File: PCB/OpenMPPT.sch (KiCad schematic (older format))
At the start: 42 parts, among them J101 THERM, J103 XT60, J104 XT60, Q101 FDMS8050, Q102 FDMS8050, Q103 FDMS8050, Q104 FDMS8050, U101 BQ24650

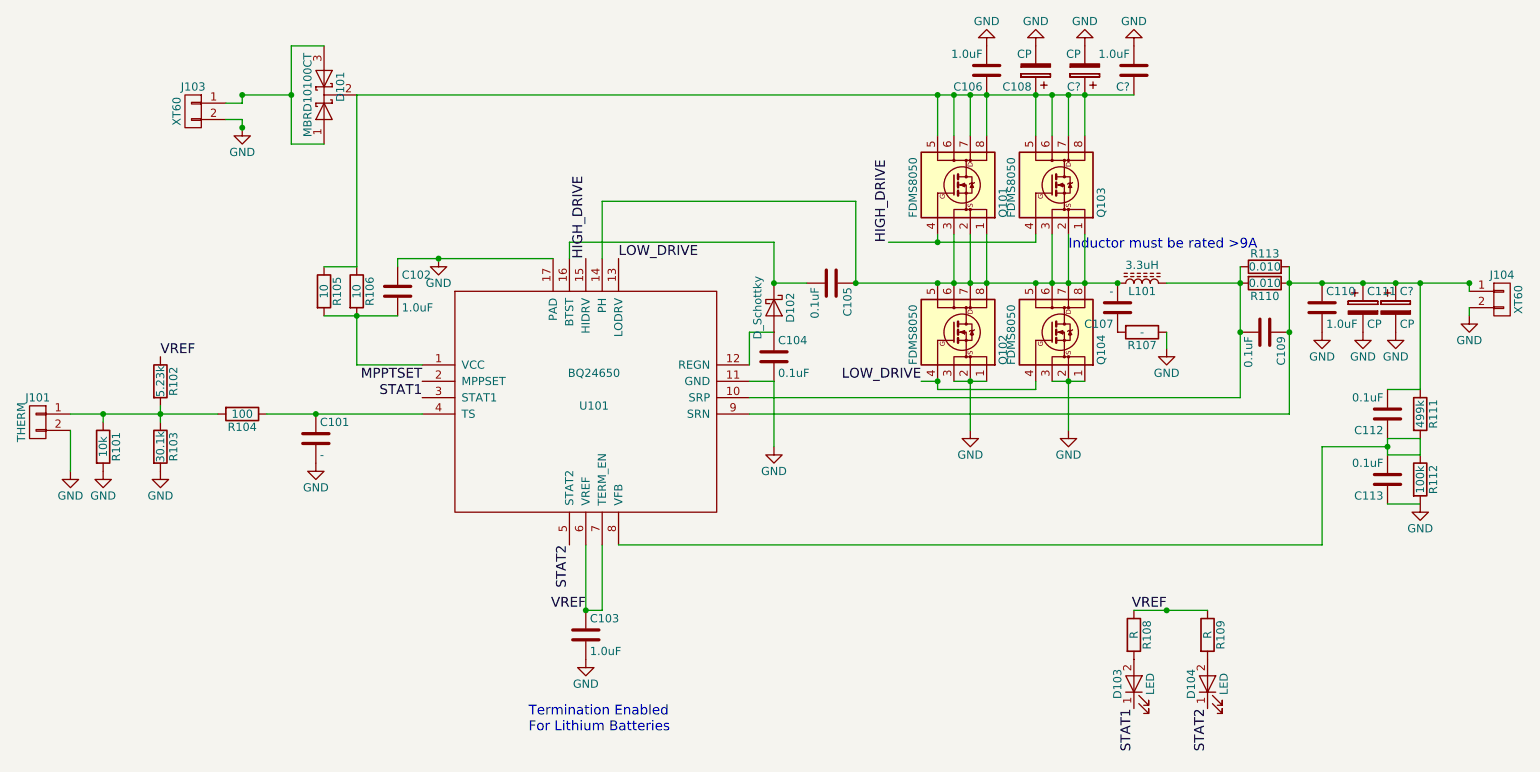
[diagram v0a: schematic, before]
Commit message: Add MPPT resistors
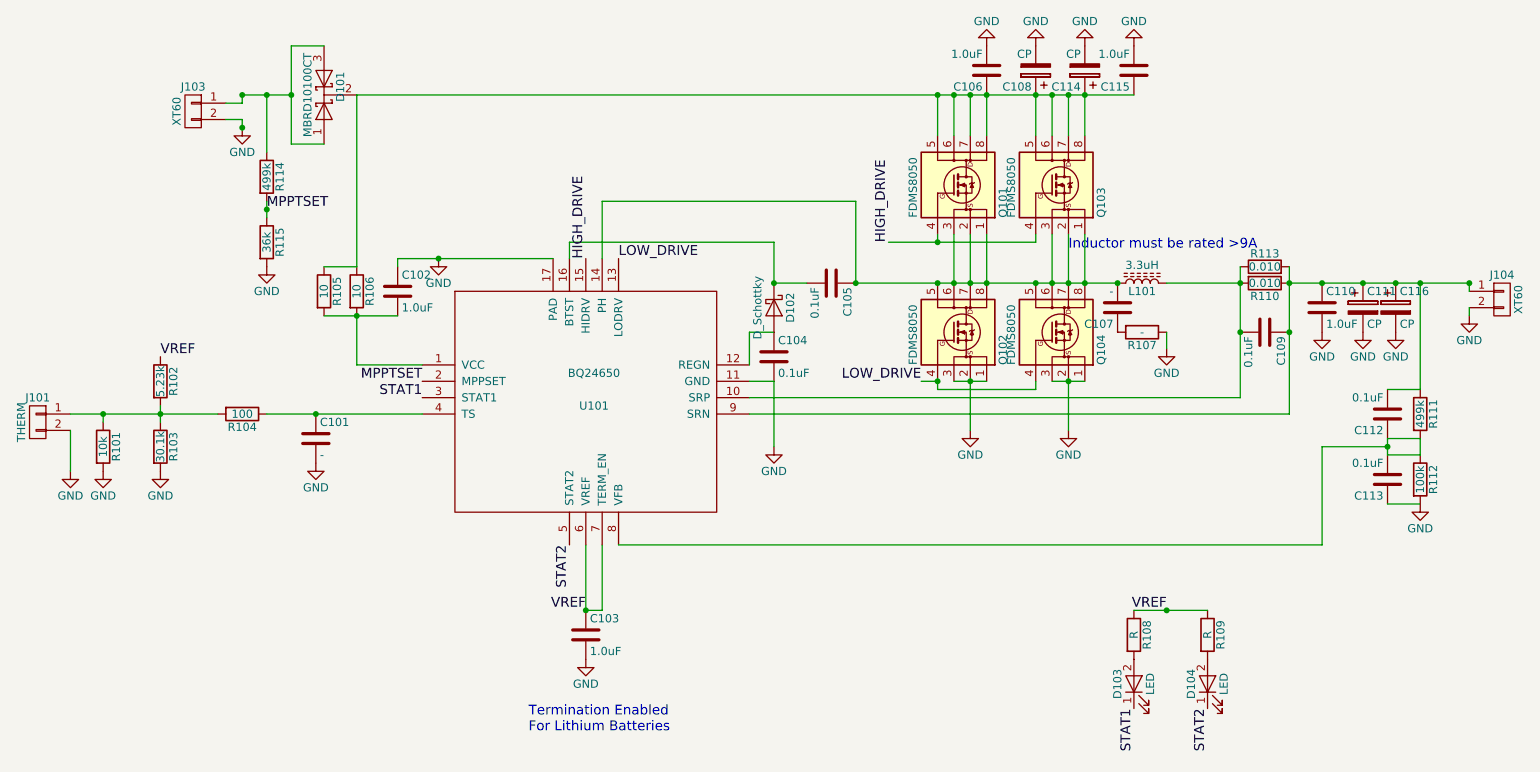
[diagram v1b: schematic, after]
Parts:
- added R114: 499k, Resistors_SMD:R_0603, symbol R
- added R115: 36k, Resistors_SMD:R_0603, symbol R
- gave numbers to parts that had none: 3
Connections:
- net GND: now also R115.2
- net MPPTSET: now also R114.2, R115.1
- net at D101.1 (A), D101.3 (A), J103.1 (P1): now also R114.1
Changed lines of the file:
@@
 $EndComp
 $Comp
-L GND #PWR106
+L GND #PWR107
 U 1 1 592922A5
 P 3800 2600
-F 0 "#PWR106" H 3800 2350 50  0001 C CNN
+F 0 "#PWR107" H 3800 2350 50  0001 C CNN
 F 1 "GND" H 3800 2450 50  0000 C CNN
 F 2 "" H 3800 2600 50  0001 C CNN
@@
 $EndComp
 $Comp
-L GND #PWR117
+L GND #PWR121
 U 1 1 592931C6
 P 10100 2950
-F 0 "#PWR117" H 10100 2700 50  0001 C CNN
+F 0 "#PWR121" H 10100 2700 50  0001 C CNN
 F 1 "GND" H 10100 2800 50  0000 C CNN
 F 2 "" H 10100 2950 50  0001 C CNN
@@
 $EndComp
 $Comp
-L GND #PWR105
+L GND #PWR106
 U 1 1 59293927
 P 3050 3850
-F 0 "#PWR105" H 3050 3600 50  0001 C CNN
+F 0 "#PWR106" H 3050 3600 50  0001 C CNN
 F 1 "GND" H 3050 3700 50  0000 C CNN
 F 2 "" H 3050 3850 50  0001 C CNN
@@
 VREF
 $Comp
-L GND #PWR107
+L GND #PWR108
 U 1 1 5929519C
 P 4700 5050
-F 0 "#PWR107" H 4700 4800 50  0001 C CNN
+F 0 "#PWR108" H 4700 4800 50  0001 C CNN
 F 1 "GND" H 4700 4900 50  0000 C CNN
 F 2 "" H 4700 5050 50  0001 C CNN
@@
 $EndComp
 $Comp
-L GND #PWR108
+L GND #PWR109
 U 1 1 59297612
 P 5850 3750
-F 0 "#PWR108" H 5850 3500 50  0001 C CNN
+F 0 "#PWR109" H 5850 3500 50  0001 C CNN
 F 1 "GND" H 5850 3600 50  0000 C CNN
 F 2 "" H 5850 3750 50  0001 C CNN
@@
 $EndComp
 $Comp
-L GND #PWR109
+L GND #PWR110
 U 1 1 5929A88C
 P 7050 3650
-F 0 "#PWR109" H 7050 3400 50  0001 C CNN
+F 0 "#PWR110" H 7050 3400 50  0001 C CNN
 F 1 "GND" H 7050 3500 50  0000 C CNN
 F 2 "" H 7050 3650 50  0001 C CNN
@@
 $EndComp
 $Comp
-L GND #PWR111
+L GND #PWR112
 U 1 1 5929C0E2
 P 7450 1300
-F 0 "#PWR111" H 7450 1050 50  0001 C CNN
+F 0 "#PWR112" H 7450 1050 50  0001 C CNN
 F 1 "GND" H 7450 1150 50  0000 C CNN
 F 2 "" H 7450 1300 50  0001 C CNN
@@
 $EndComp
 $Comp
-L GND #PWR113
+L GND #PWR116
 U 1 1 5929C9CE
 P 8250 3150
-F 0 "#PWR113" H 8250 2900 50  0001 C CNN
+F 0 "#PWR116" H 8250 2900 50  0001 C CNN
 F 1 "GND" H 8250 3000 50  0000 C CNN
 F 2 "" H 8250 3150 50  0001 C CNN
@@
 $EndComp
 $Comp
-L GND #PWR114
+L GND #PWR117
 U 1 1 5929D1D8
 P 9200 3050
-F 0 "#PWR114" H 9200 2800 50  0001 C CNN
+F 0 "#PWR117" H 9200 2800 50  0001 C CNN
 F 1 "GND" H 9200 2900 50  0000 C CNN
 F 2 "" H 9200 3050 50  0001 C CNN
@@
 $EndComp
 $Comp
-L GND #PWR110
+L GND #PWR111
 U 1 1 5929DA52
 P 7150 1300
-F 0 "#PWR110" H 7150 1050 50  0001 C CNN
+F 0 "#PWR111" H 7150 1050 50  0001 C CNN
 F 1 "GND" H 7150 1150 50  0000 C CNN
 F 2 "" H 7150 1300 50  0001 C CNN
@@
 $EndComp
 $Comp
-L GND #PWR116
+L GND #PWR120
 U 1 1 5929EA7A
 P 9800 4100
-F 0 "#PWR116" H 9800 3850 50  0001 C CNN
+F 0 "#PWR120" H 9800 3850 50  0001 C CNN
 F 1 "GND" H 9800 3950 50  0000 C CNN
 F 2 "" H 9800 4100 50  0001 C CNN
@@
 $EndComp
 $Comp
-L GND #PWR112
+L GND #PWR113
 U 1 1 59296657
 P 7650 3650
-F 0 "#PWR112" H 7650 3400 50  0001 C CNN
+F 0 "#PWR113" H 7650 3400 50  0001 C CNN
 F 1 "GND" H 7650 3500 50  0000 C CNN
 F 2 "" H 7650 3650 50  0001 C CNN
@@
 $EndComp
 $Comp
-L GND #PWR115
+L GND #PWR118
 U 1 1 592982F3
 P 9450 3050
-F 0 "#PWR115" H 9450 2800 50  0001 C CNN
+F 0 "#PWR118" H 9450 2800 50  0001 C CNN
 F 1 "GND" H 9450 2900 50  0000 C CNN
 F 2 "" H 9450 3050 50  0001 C CNN
@@
 $EndComp
 $Comp
-L CP C?
+L CP C114
 U 1 1 5929B387
 P 7750 1450
-F 0 "C?" H 7775 1550 50  0000 L CNN
+F 0 "C114" H 7775 1550 50  0000 L CNN
 F 1 "CP" H 7775 1350 50  0000 L CNN
 F 2 "Capacitors_SMD:CP_Elec_6.3x7.7" H 7788 1300 50  0001 C CNN
@@
 $EndComp
 $Comp
-L GND #PWR?
+L GND #PWR114
 U 1 1 5929B418
 P 7750 1300
-F 0 "#PWR?" H 7750 1050 50  0001 C CNN
+F 0 "#PWR114" H 7750 1050 50  0001 C CNN
 F 1 "GND" H 7750 1150 50  0000 C CNN
 F 2 "" H 7750 1300 50  0001 C CNN
@@
 $EndComp
 $Comp
-L C C?
+L C C115
 U 1 1 5929B49B
 P 8050 1450
-F 0 "C?" H 8075 1550 50  0000 L CNN
+F 0 "C115" H 8075 1550 50  0000 L CNN
 F 1 "1.0uF" H 8075 1350 50  0000 L CNN
 F 2 "Capacitors_SMD:C_0805" H 8088 1300 50  0001 C CNN
@@
 $EndComp
 $Comp
-L GND #PWR?
+L GND #PWR115
 U 1 1 5929B542
 P 8050 1300
-F 0 "#PWR?" H 8050 1050 50  0001 C CNN
+F 0 "#PWR115" H 8050 1050 50  0001 C CNN
 F 1 "GND" H 8050 1150 50  0000 C CNN
 F 2 "" H 8050 1300 50  0001 C CNN
@@
 Connection ~ 7750 1600
 $Comp
-L CP C?
+L CP C116
 U 1 1 5929B9C5
 P 9650 2900
-F 0 "C?" H 9675 3000 50  0000 L CNN
+F 0 "C116" H 9675 3000 50  0000 L CNN
 F 1 "CP" H 9675 2800 50  0000 L CNN
 F 2 "Capacitors_SMD:CP_Elec_6.3x7.7" H 9688 2750 50  0001 C CNN
@@
 $EndComp
 $Comp
-L GND #PWR?
+L GND #PWR119
 U 1 1 5929BA5C
 P 9650 3050
-F 0 "#PWR?" H 9650 2800 50  0001 C CNN
+F 0 "#PWR119" H 9650 2800 50  0001 C CNN
 F 1 "GND" H 9650 2900 50  0000 C CNN
 F 2 "" H 9650 3050 50  0001 C CNN
@@
 $EndComp
 Connection ~ 9650 2750
+$Comp
+L R R114
+U 1 1 592956D5
+P 2750 2100
+F 0 "R114" V 2830 2100 50  0000 C CNN
+F 1 "499k" V 2750 2100 50  0000 C CNN
+F 2 "Resistors_SMD:R_0603" V 2680 2100 50  0001 C CNN
+F 3 "" H 2750 2100 50  0001 C CNN
+	1    2750 2100
+	1    0    0    -1
+$EndComp
+$Comp
+L R R115
+U 1 1 59295784
+P 2750 2500
+F 0 "R115" V 2830 2500 50  0000 C CNN
+F 1 "36k" V 2750 2500 50  0000 C CNN
+F 2 "Resistors_SMD:R_0603" V 2680 2500 50  0001 C CNN
+F 3 "" H 2750 2500 50  0001 C CNN
+	1    2750 2500
+	1    0    0    -1
+$EndComp
+Wire Wire Line
+	2750 2250 2750 2350
+Wire Wire Line
+	2750 1950 2750 1600
+Connection ~ 2750 1600
+$Comp
+L GND #PWR105
+U 1 1 5929597A
+P 2750 2650
+F 0 "#PWR105" H 2750 2400 50  0001 C CNN
+F 1 "GND" H 2750 2500 50  0000 C CNN
+F 2 "" H 2750 2650 50  0001 C CNN
+F 3 "" H 2750 2650 50  0001 C CNN
+	1    2750 2650
+	1    0    0    -1
+$EndComp
+Text Label 2750 2300 0    60   ~ 0
+MPPTSET
+Connection ~ 2750 2300
 $EndSCHEMATC

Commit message: Finish Routing
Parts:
- removed R104: 100, Resistors_SMD:R_0603, symbol R
- removed R107: -, Resistors_SMD:R_0603, symbol R
- C102, C103, C106, C110: bom_partno (none) -> CL10A105KB8NNNC
- C104, C105, C109, C112, C113: bom_partno (none) -> CC0603ZRY5V9BB104
- C107: value - -> 1.0uF; bom_partno (none) -> CL10A105KB8NNNC
- D101: bom_partno (none) -> MBRD10100CTTR
- D102: footprint (none) -> Diodes_SMD:D_SOD-523; bom_partno (none) -> ZLLS350TA
- J103, J104: footprint xt60:XT60 -> xt60:XT30PW_Male
- Q101, Q102, Q103, Q104: bom_partno (none) -> AON7400B
- R101: bom_partno (none) -> NTCG163JH103JT1
- R102: bom_partno (none) -> RMCF0603FT5K23
- R103: bom_partno (none) -> RMCF0603FT30K1
- R105: value 10 -> -
- R106: bom_partno (none) -> RC0603JR-0710RL
- R108, R109: value R -> 5.23k; bom_partno (none) -> RMCF0603FT5K23
- R110: bom_partno (none) -> KRL3264-C-R010-F-T1
- R111, R114: bom_partno (none) -> RMCF0603FT499K
- R112: bom_partno (none) -> RC0603JR-07100KL
- R113: bom_partno - -> KRL3264-C-R010-F-T1
- R115: bom_partno (none) -> ERJ-3GEYJ363V
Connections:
- net GND: now also C107.2
- net at C104.1, D102.2 (A), U101.12 (REGN): now also C107.1
- net at C105.1, L101.1, Q101.1 (S)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: no longer C107.2
- net at C101.1, U101.4 (TS): now also J101.1 (P1), R101.1, R102.2, R103.1
